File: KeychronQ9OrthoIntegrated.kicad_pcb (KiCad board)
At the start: 2 copper layers, 309.6 x 76.2 mm, 164 parts, among them J1 Conn_01x07, J3 Conn_01x05, SW1 RotaryEncoder_Switch, SW2 RotaryEncoder_Switch, U1 XC6206PxxxMR, U2 SRV05-4, U3 RP2040, U4 W25Q128JVS, Y1 Crystal_GND24

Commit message: fix silkscreen/solder mask conflicts
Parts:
- D1, D10, D11, D12, D13, D14, D15, D16, D17, D18, D19, D2, D20, D21, D22, D23, D24, D25, D26, D27, D28, D29, D3, D30, D31, D32, D33, D34, D35, D36, D37, D38, D39, D4, D40, D41, D42, D43, D44, D45, D46, D47, D48, D49, D5, D50, D51, D52, D54, D55, D56, D57, D58, D59, D6, D61, D62, D63, D64, D65, D7, D8, D9: footprint Diode_SMD:D_SOD-123 -> xomm:D_SOD-123_xomm
- MX1, MX16, MX2, MX3, MX32, MX52, MX53, MX54, MX59, MX60, MX61: footprint PCM_marbastlib-mx:SW_MX_HS_CPG151101S11_1u -> PCM_marbastlib-mx:SW_MX_HS_S_CPG151101S11_1u
- moved C13 0.86 mm to (306.7, 70.2)
- moved C10 0.61 mm to (309.6, 74.5)
- moved C12 0.61 mm to (306.0, 74.7)
- moved Y1 0.61 mm to (308.0, 72.9)
- moved R9 0.60 mm to (305.0, 72.7)
- moved R5 0.39 mm to (298.8, 72.5)
- moved C4 0.09 mm to (305.5, 70.1)
- moved D16 0.09 mm to (319.0, 26.2)
- moved D32 0.09 mm to (319.0, 50.0)
- moved D65 0.09 mm to (314.2, 83.3)
- moved D15 0.09 mm to (295.2, 26.2)
- moved D31 0.09 mm to (295.2, 45.2)
- moved D47 0.09 mm to (295.2, 64.3)
- moved D64 0.09 mm to (295.2, 83.3)
- moved D14 0.09 mm to (276.1, 26.2)
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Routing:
- net +3V3: track 145.6 -> 174.6 mm, vias 3 -> 5
- net SWD: track 25.5 -> 28.4 mm
- net SWC: track 28.1 -> 31.0 mm
- net GND: track 108.4 -> 110.2 mm, vias 57 -> 62
- net RESET: track 38.9 -> 39.9 mm
- net XIN: track 8.44 -> 7.83 mm

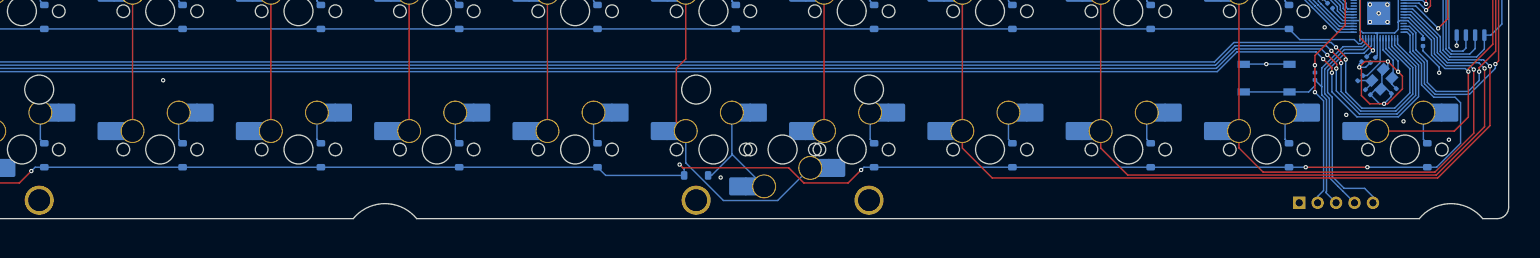
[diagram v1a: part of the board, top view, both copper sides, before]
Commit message: add back right side numpad layout
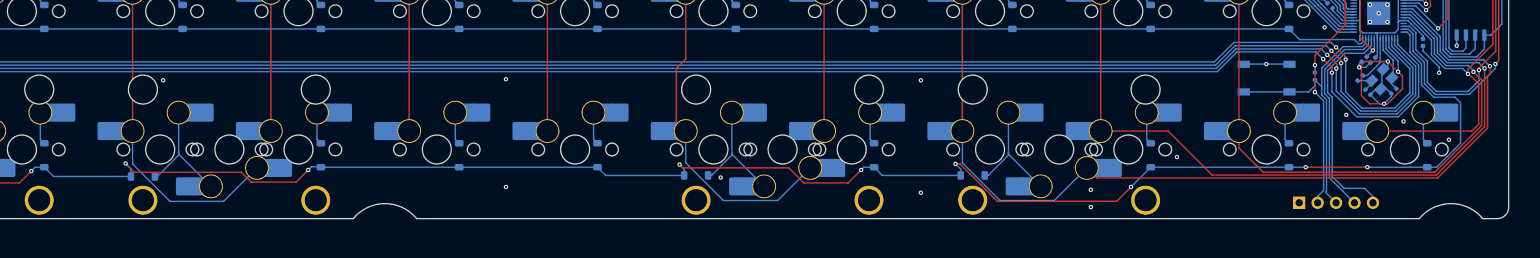
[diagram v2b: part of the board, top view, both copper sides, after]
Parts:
- added MX66: MX_SW_HS, PCM_marbastlib-mx:SW_MX_HS_S_CPG151101S11_1u, B.Cu at (149.2, 82.5)
- added MX67: MX_SW_HS, PCM_marbastlib-mx:SW_MX_HS_S_CPG151101S11_1u, B.Cu at (263.5, 82.5)
- added S3: MX_stab, PCM_marbastlib-mx:STAB_MX_P_2u, F.Cu at (149.2, 82.5)
- added S4: MX_stab, PCM_marbastlib-mx:STAB_MX_P_2u, F.Cu at (263.5, 82.5)
- MX55, MX56, MX62, MX63: footprint PCM_marbastlib-mx:SW_MX_HS_CPG151101S11_1u -> PCM_marbastlib-mx:SW_MX_HS_S_CPG151101S11_1u
- moved D55 6.20 mm to (137.3, 86.3), turned to 0 degrees
- moved D62 6.13 mm to (251.6, 86.1), turned to 0 degrees
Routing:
- net Col 7: track 238.5 -> 264.2 mm
- net Net-(D55-A): track 4.45 -> 17.0 mm
- net Row 4: track 322.2 -> 334.7 mm, vias 6 -> 10
- net Net-(D62-A): track 4.45 -> 16.8 mm
- net Col 13: track 161.4 -> 166.3 mm
- net Col 16: track 367.1 -> 369.9 mm
- net Col 14: track 140.3 -> 138.9 mm
- net Col 15: track 118.2 -> 119.0 mm
- net GND: vias 62 -> 69

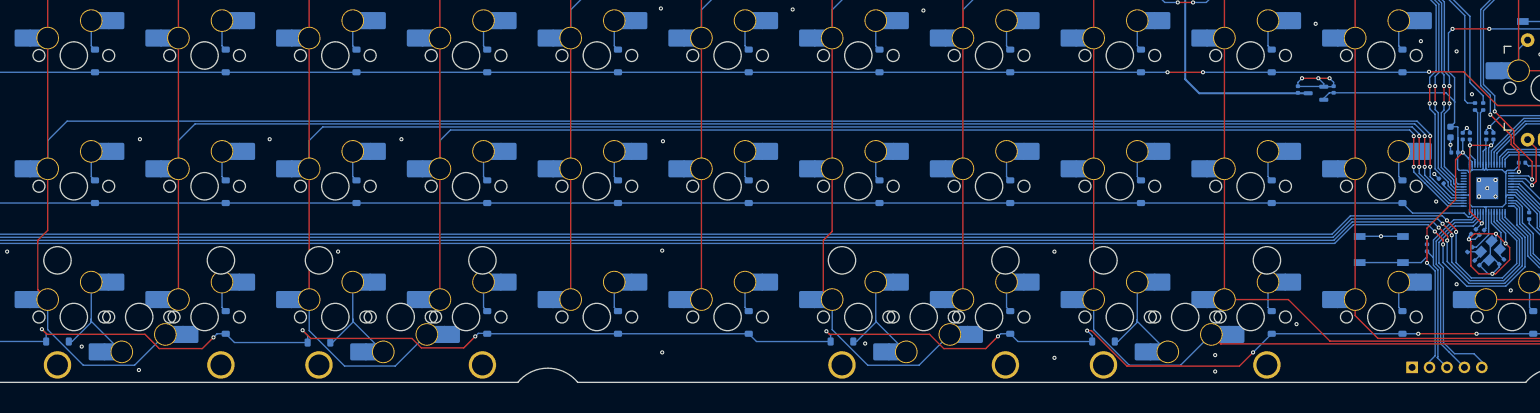
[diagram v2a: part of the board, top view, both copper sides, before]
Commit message: fix spacebar routing
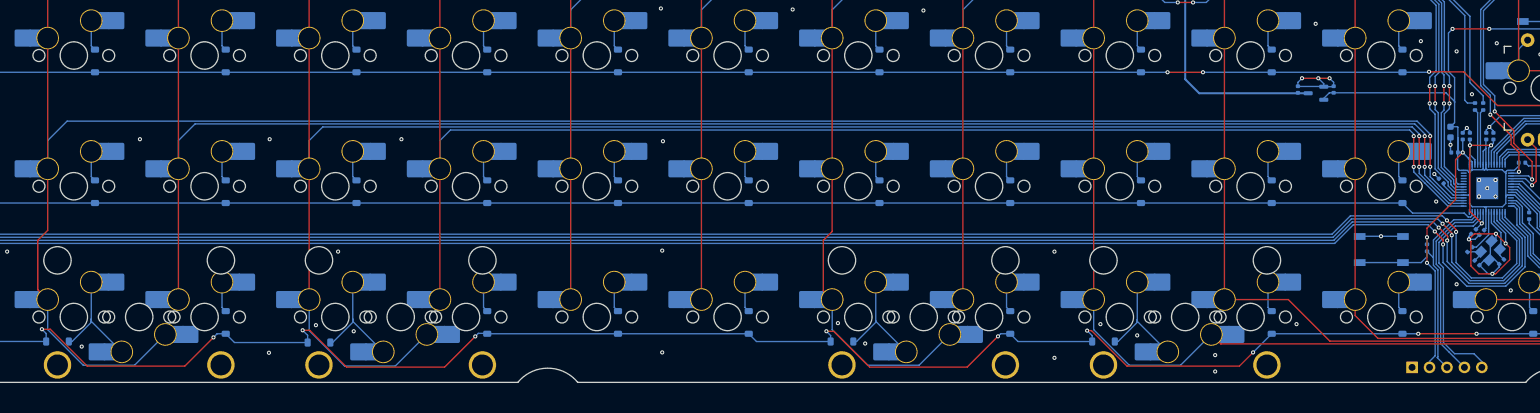
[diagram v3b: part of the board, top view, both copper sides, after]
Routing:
- net Row 4: track 334.7 -> 341.4 mm
- net GND: vias 69 -> 75
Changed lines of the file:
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@@
 	)
 	(via
+		(at 212.923272 83.442912)
+		(size 0.6)
+		(drill 0.3)
+		(layers "F.Cu" "B.Cu")
+		(free yes)
+		(net 2)
+	)
+	(via
+		(at 308.917332 42.66404)
+		(size 0.6)
+		(drill 0.3)
+		(layers "F.Cu" "B.Cu")
+		(free yes)
+		(net 2)
+	)
+	(via
 		(at 187.324856 72.876124)
 		(size 0.6)
@@
 	)
 	(via
+		(at 130.026076 87.758924)
+		(size 0.6)
+		(drill 0.3)
+		(layers "F.Cu" "B.Cu")
+		(free yes)
+		(net 2)
+	)
+	(via
+		(at 251.172068 83.59174)
+		(size 0.6)
+		(drill 0.3)
+		(layers "F.Cu" "B.Cu")
+		(free yes)
+		(net 2)
+	)
+	(via
 		(at 305.302088 50.099176)
 		(size 0.6)
@@
 	)
 	(via
+		(at 136.872164 83.740568)
+		(size 0.6)
+		(drill 0.3)
+		(layers "F.Cu" "B.Cu")
+		(free yes)
+		(net 2)
+	)
+	(via
 		(at 307.832164 54.861672)
 		(size 0.6)
@@
 	)
 	(via
+		(at 256.529876 85.228848)
+		(size 0.6)
+		(drill 0.3)
+		(layers "F.Cu" "B.Cu")
+		(free yes)
+		(net 2)
+	)
+	(via
 		(at 48.722616 31.19802)
 		(size 0.6)
@@
 	)
 	(via
-		(at 111.081548 90.282736)
-		(size 0.6)
-		(drill 0.3)
-		(layers "F.Cu" "B.Cu")
-		(free yes)
-		(net 2)
-	)
-	(via
 		(at 36.965204 35.960516)
 		(size 0.6)
@@
 	)
 	(via
+		(at 142.3788 84.633536)
+		(size 0.6)
+		(drill 0.3)
+		(layers "F.Cu" "B.Cu")
+		(free yes)
+		(net 2)
+	)
+	(via
 		(at 244.475 88.503125)
 		(size 0.6)
@@
 	)
 	(segment
-		(start 136.132692 85.68)
-		(end 150.867283 85.68)
+		(start 231.774792 89.842516)
+		(end 236.245896 85.371412)
 		(width 0.2)
 		(layer "F.Cu")
@@
 	)
 	(segment
-		(start 234.45996 87.157348)
-		(end 228.358012 87.157348)
+		(start 117.772544 89.693688)
+		(end 103.534692 89.693688)
 		(width 0.2)
 		(layer "F.Cu")
@@
 	)
 	(segment
-		(start 228.358012 87.157348)
-		(end 226.27442 85.073756)
+		(start 141.337004 89.842516)
+		(end 155.624492 89.842516)
 		(width 0.2)
 		(layer "F.Cu")
@@
 	)
 	(segment
-		(start 297.483026 84.99375)
-		(end 305.977406 84.99375)
+		(start 103.534692 89.693688)
+		(end 98.176884 84.33588)
 		(width 0.2)
 		(layer "F.Cu")
@@
 	)
 	(segment
-		(start 134.9374 84.484708)
-		(end 136.132692 85.68)
+		(start 155.624492 89.842516)
+		(end 160.089332 85.377676)
 		(width 0.2)
 		(layer "F.Cu")
@@
 	)
 	(segment
-		(start 255.029984 89.69375)
-		(end 271.4318 89.69375)
+		(start 135.979196 84.484708)
+		(end 141.337004 89.842516)
 		(width 0.2)
 		(layer "F.Cu")
@@
 	)
 	(segment
-		(start 236.245896 85.371412)
-		(end 234.45996 87.157348)
+		(start 297.483026 84.99375)
+		(end 305.977406 84.99375)
 		(width 0.2)
 		(layer "F.Cu")
@@
 	)
 	(segment
-		(start 97.687028 85.073756)
-		(end 96.942888 84.329616)
+		(start 255.029984 89.69375)
+		(end 271.4318 89.69375)
 		(width 0.2)
 		(layer "F.Cu")
@@
 	)
 	(segment
-		(start 111.974516 85.073756)
-		(end 97.687028 85.073756)
+		(start 211.242792 84.627272)
+		(end 211.249056 84.633536)
 		(width 0.2)
 		(layer "F.Cu")
@@
 	)
 	(segment
-		(start 249.2375 84.534375)
-		(end 249.870609 84.534375)
+		(start 98.176884 84.33588)
+		(end 96.949152 84.33588)
 		(width 0.2)
 		(layer "F.Cu")
@@
 	)
 	(segment
-		(start 211.689276 85.073756)
-		(end 211.242792 84.627272)
-		(width 0.2)
-		(layer "F.Cu")
-		(net 96)
-	)
-	(segment
-		(start 121.945992 85.52024)
-		(end 120.308884 87.157348)
+		(start 249.2375 84.534375)
+		(end 249.870609 84.534375)
 		(width 0.2)
 		(layer "F.Cu")
@@
 	)
 	(segment
-		(start 152.227283 87.04)
-		(end 158.427008 87.04)
+		(start 134.9374 84.484708)
+		(end 135.979196 84.484708)
 		(width 0.2)
 		(layer "F.Cu")
@@
 	)
 	(segment
-		(start 114.058108 87.157348)
-		(end 111.974516 85.073756)
+		(start 271.4318 89.69375)
+		(end 273.416175 87.709375)
 		(width 0.2)
 		(layer "F.Cu")
@@
 	)
 	(segment
-		(start 271.4318 89.69375)
-		(end 273.416175 87.709375)
+		(start 211.249056 84.633536)
+		(end 212.32796 84.633536)
 		(width 0.2)
 		(layer "F.Cu")
@@
 	)
 	(segment
-		(start 150.867283 85.68)
-		(end 152.227283 87.04)
+		(start 217.53694 89.842516)
+		(end 231.774792 89.842516)
 		(width 0.2)
 		(layer "F.Cu")
@@
 	)
 	(segment
-		(start 158.427008 87.04)
-		(end 160.089332 85.377676)
+		(start 212.32796 84.633536)
+		(end 217.53694 89.842516)
 		(width 0.2)
 		(layer "F.Cu")
@@
 	)
 	(segment
-		(start 226.27442 85.073756)
-		(end 211.689276 85.073756)
+		(start 121.945992 85.52024)
+		(end 117.772544 89.693688)
 		(width 0.2)
 		(layer "F.Cu")
@@
 	)
 	(segment
-		(start 120.308884 87.157348)
-		(end 114.058108 87.157348)
+		(start 96.949152 84.33588)
+		(end 96.942888 84.329616)
 		(width 0.2)
 		(layer "F.Cu")
